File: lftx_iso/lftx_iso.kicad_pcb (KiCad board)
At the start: 2 copper layers, 9 parts, among them P1 CONN_01X02, P2 CONN_02X08, P3 CONN_02X08, U1 ADUM5402ARWZ

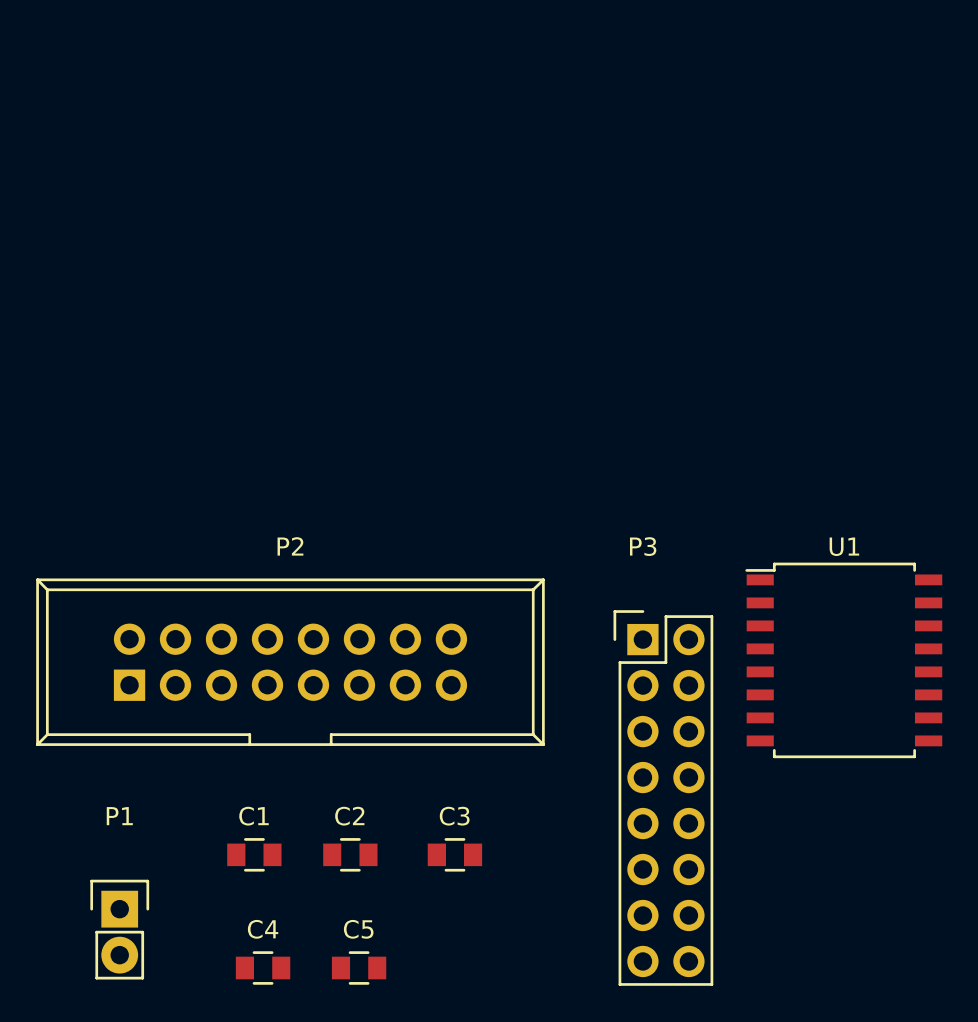
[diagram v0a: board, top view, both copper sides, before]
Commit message: moved headers on isolation boards to match actual measurements on lfrx and lftx usrp daughterboards, ready to order
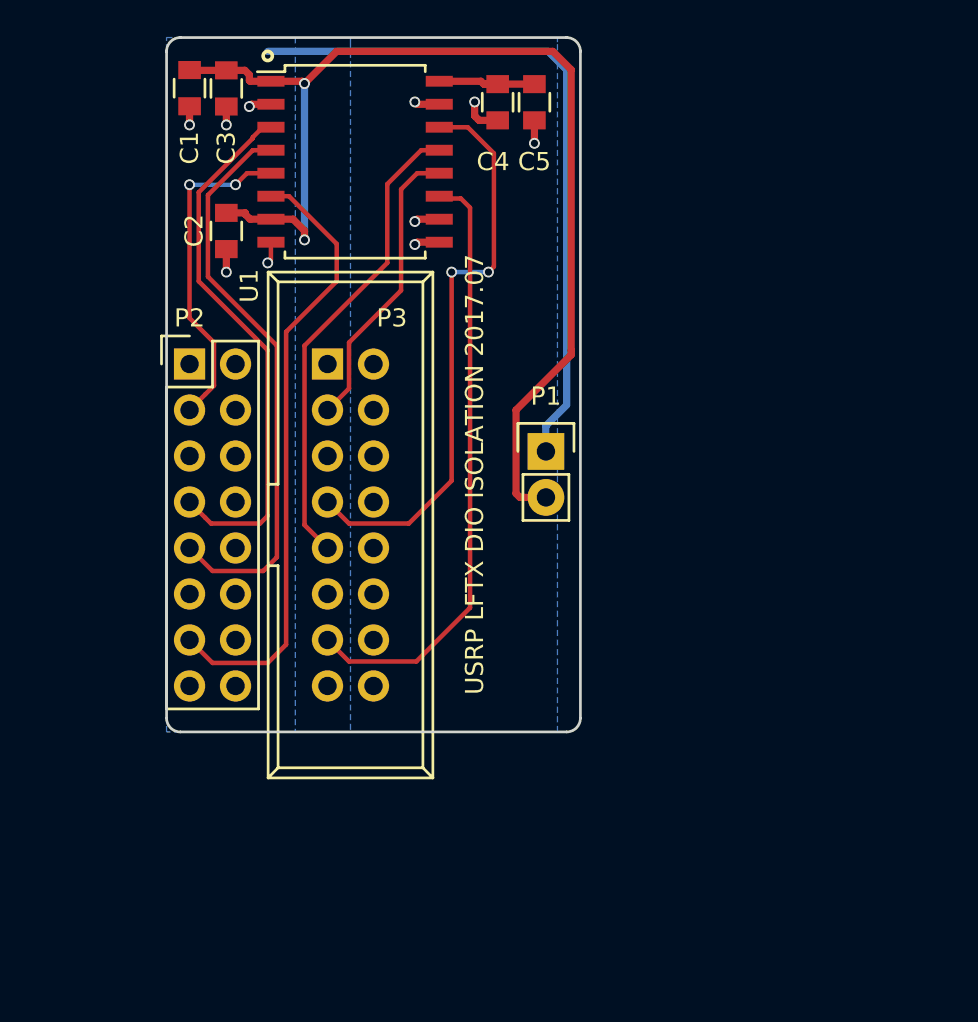
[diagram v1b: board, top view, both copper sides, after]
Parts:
- P2: footprint Connect:IDC_Header_Straight_16pins -> Pin_Headers:Pin_Header_Straight_2x08
- P3: footprint Pin_Headers:Pin_Header_Straight_2x08 -> Connect:IDC_Header_Straight_16pins
- moved C4 49.5 mm to (217.7, 47.5), turned to 270 degrees
- moved C5 48.8 mm to (219.7, 47.5), turned to 270 degrees
- moved C3 44.2 mm to (202.7, 46.8), turned to 270 degrees
- moved C1 42.5 mm to (200.7, 46.7), turned to 270 degrees
- moved U1 38.6 mm to (209.8, 50.8)
- moved C2 35.1 mm to (202.7, 54.6), turned to 270 degrees
- moved P1 34.5 mm to (220.3, 66.8)
- moved P3 23.1 mm to (208.3, 62.0), turned to 270 degrees
- moved P2 18.0 mm to (200.7, 62.0)
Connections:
- P2 pad 1: Net-(P2-Pad1) -> (no net)
- P2 pad 11: Net-(P2-Pad11) -> (no net)
- P2 pad 15: Net-(P2-Pad15) -> (no net)
- P2 pad 5: Net-(P2-Pad5) -> (no net)
- P3 pad 1: Net-(P3-Pad1) -> (no net)
- P3 pad 11: Net-(P3-Pad11) -> (no net)
- P3 pad 15: Net-(P3-Pad15) -> (no net)
- P3 pad 5: Net-(P3-Pad5) -> (no net)
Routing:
- net +3V3: track 0.00 -> 63.1 mm, vias 0 -> 2
- net GND: track 0.00 -> 44.3 mm, vias 0 -> 5
- net /DISABLE: track 0.00 -> 34.3 mm
- net /DISABLE_ISO: track 0.00 -> 33.7 mm
- net /TRA_ISO: track 0.00 -> 32.2 mm, vias 0 -> 2
- net /TRB: track 0.00 -> 31.8 mm
- net /TRA: track 0.00 -> 29.9 mm
- net /TRB_ISO: track 0.00 -> 26.2 mm
- net /FAULT: track 0.00 -> 18.3 mm, vias 0 -> 2
- net /FAULT_ISO: track 0.00 -> 16.4 mm
- net GNDA: track 0.00 -> 7.61 mm, vias 0 -> 5
- net VDDA: track 0.00 -> 5.58 mm
- added copper zone on B.Cu, net GND
- added copper zone on B.Cu, net GNDA
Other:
- board outline added: 22.9 x 38.4 mm
- board text added: "USRP LFTX DIO ISOLATION 2017.07"

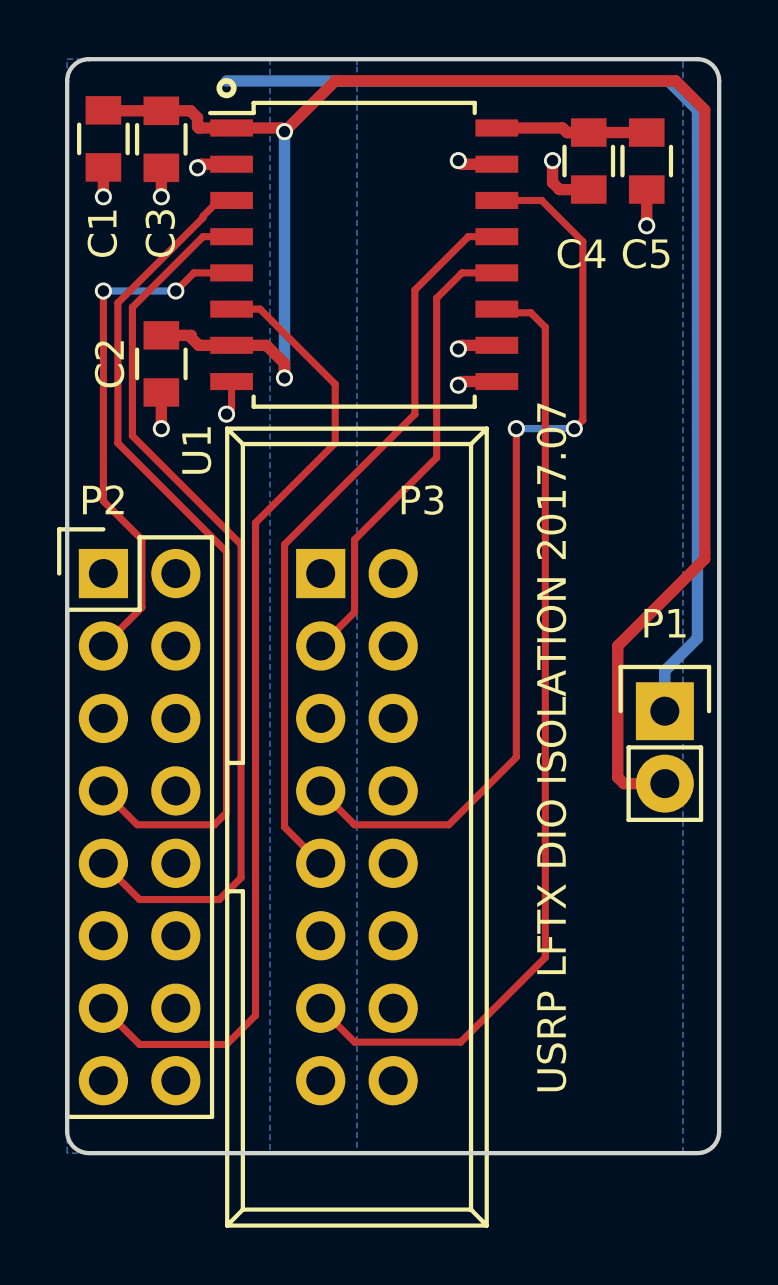
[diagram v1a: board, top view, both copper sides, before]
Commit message: dfm changes to isolation boards, increased annual ring size and copper to edge clearance. ordered boards
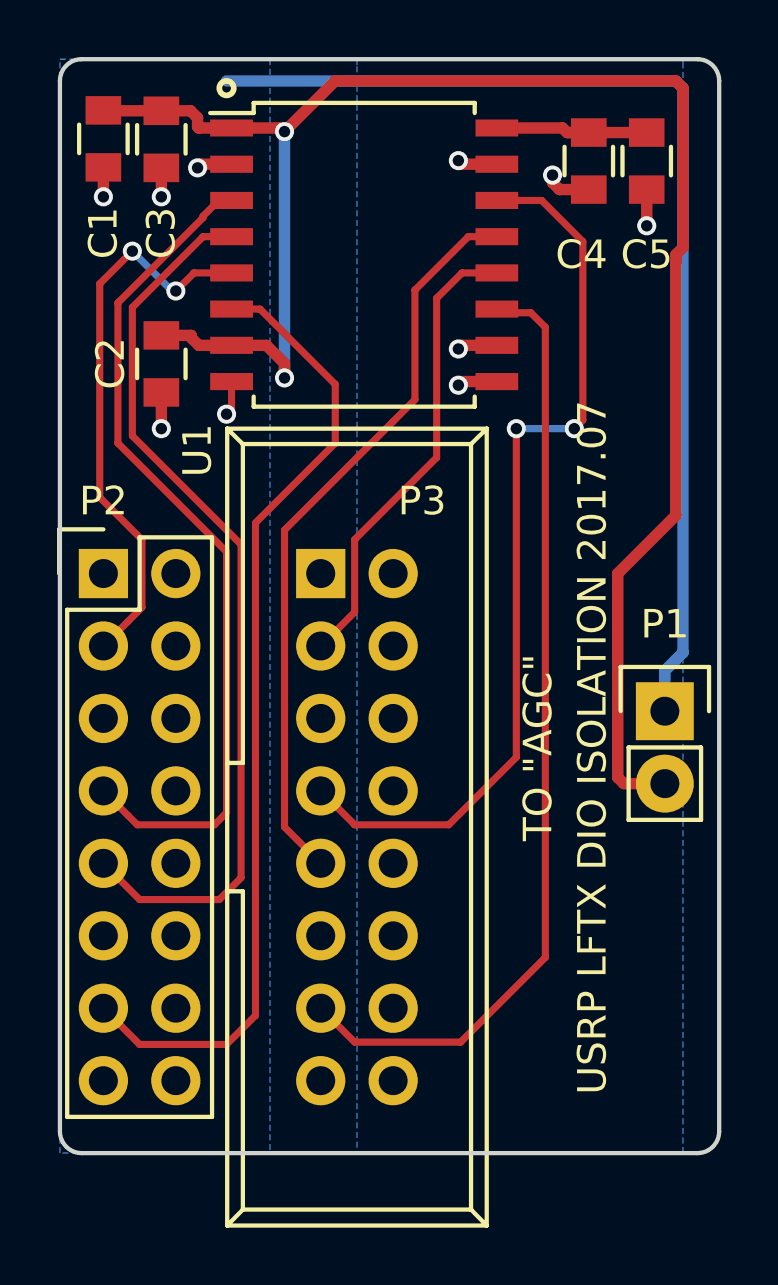
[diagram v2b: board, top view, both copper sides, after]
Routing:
- net /FAULT: track 18.3 -> 19.8 mm
- net +3V3: track 63.1 -> 62.4 mm
- net GNDA: track 7.61 -> 7.11 mm
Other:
- board size 22.9 x 38.4 mm -> 23.1 x 38.4 mm
- net class Default: via_dia 0.6 -> 0.67
- board text added: "TO "AGC""

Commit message: added rf-front end module for mcmurdo USRP upgrade
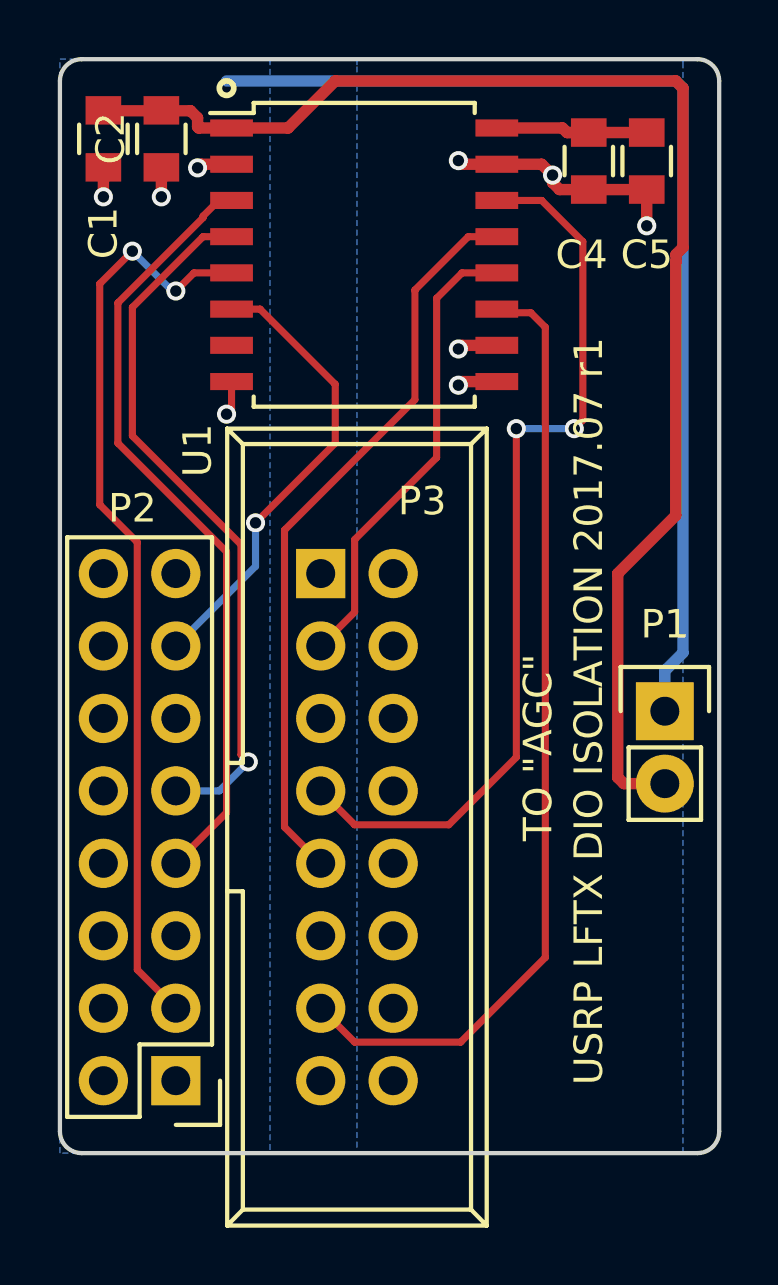
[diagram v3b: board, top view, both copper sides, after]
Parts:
- removed C3: 100 nF, Capacitors_SMD:C_0805
- moved P2 18.0 mm to (203.2, 79.8), turned to 180 degrees
- moved C2 7.89 mm to (202.7, 46.7)
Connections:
- P2 pad 1: (no net) -> Net-(P2-Pad1)
- P2 pad 11: (no net) -> Net-(P2-Pad11)
- P2 pad 15: (no net) -> Net-(P2-Pad15)
- P2 pad 5: (no net) -> Net-(P2-Pad5)
- P3 pad 1: (no net) -> Net-(P3-Pad1)
- P3 pad 11: (no net) -> Net-(P3-Pad11)
- P3 pad 15: (no net) -> Net-(P3-Pad15)
- P3 pad 5: (no net) -> Net-(P3-Pad5)
- U1 pad 7: +3V3 -> Net-(U1-Pad7)
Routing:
- net /DISABLE: track 34.3 -> 16.6 mm, vias 0 -> 1
- net +3V3: track 62.4 -> 48.4 mm, vias 2 -> 0
- net /FAULT: track 19.8 -> 32.4 mm
- net /TRB: track 31.8 -> 25.1 mm, vias 0 -> 1
- net GNDA: track 7.11 -> 11.3 mm
- net /TRA: track 29.9 -> 27.5 mm
- net GND: track 44.0 -> 42.7 mm, vias 5 -> 4
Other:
- board text added: "USRP LFTX DIO ISOLATION 2017.07 r1"
- board text removed: "USRP LFTX DIO ISOLATION 2017.07"
